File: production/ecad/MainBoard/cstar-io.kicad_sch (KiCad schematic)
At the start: 8 parts, among them J1 691137710002, J5 Conn_01x04_Socket, Q2 AO3400A, Q8 IRFHM9331TRPBF

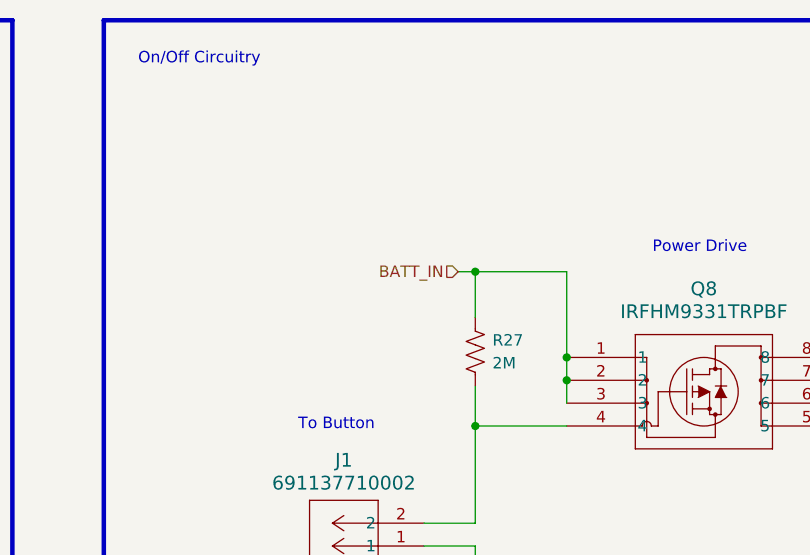
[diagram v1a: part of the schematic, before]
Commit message: updated battery connection net name
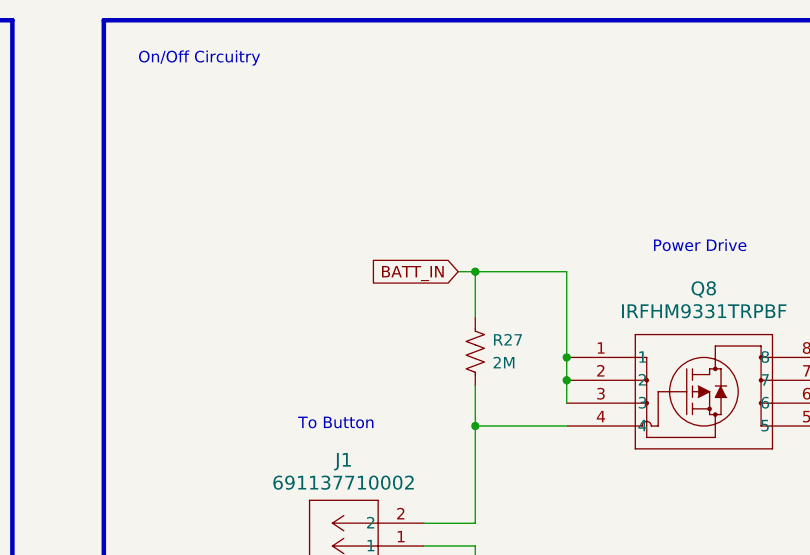
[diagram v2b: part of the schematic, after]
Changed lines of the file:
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@@
     (effects (font (size 1.27 1.27)) (justify left bottom))
+  )
+  (global_label "BATT_IN" (shape input) (at 196.85 43.815 180) (fields_autoplaced)
+    (effects (font (size 1.27 1.27)) (justify right))
+    (property "Intersheetrefs" "${INTERSHEET_REFS}" (at 186.6681 43.815 0)
+      (effects (font (size 1.27 1.27)) (justify right) hide)
+    )
   )
   (hierarchical_label "RGB_Red_Control" (shape input) (at 45.085 54.61 180) (fields_autoplaced)
@@
     (effects (font (size 1.27 1.27)) (justify right))
   )
-  (hierarchical_label "BATT_IN" (shape input) (at 196.85 43.815 180) (fields_autoplaced)
-    (effects (font (size 1.27 1.27)) (justify right))
-  )

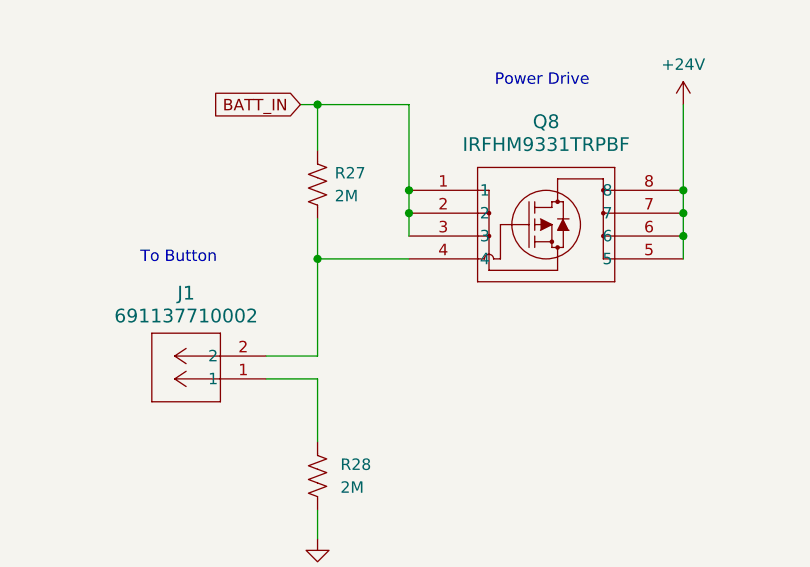
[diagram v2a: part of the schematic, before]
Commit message: added test point
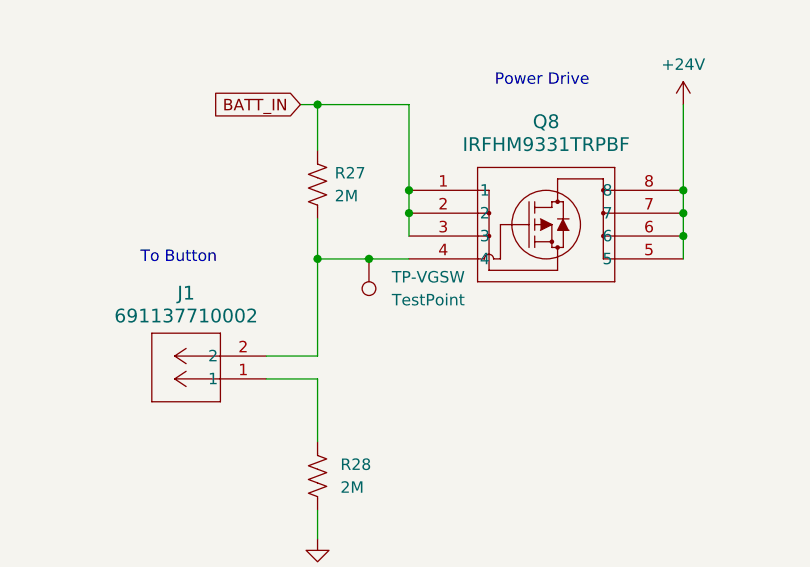
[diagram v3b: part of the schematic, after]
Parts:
- added TP-VGSW: TestPoint, symbol Connector:TestPoint
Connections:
- net at J1.2, Q8.4, R27.2: now also TP-VGSW.1
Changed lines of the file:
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@@
   (junction (at 239.395 55.88) (diameter 0) (color 0 0 0 0)
   )
+  (junction (at 204.47 60.96) (diameter 0) (color 0 0 0 0)
+  )
   (junction (at 208.915 55.88) (diameter 0) (color 0 0 0 0)
   )
@@
     (stroke (width 0.5) (type default))
   )
-  (wire (pts (xy 198.755 60.96) (xy 208.915 60.96))
+  (wire (pts (xy 198.755 60.96) (xy 204.47 60.96))
     (stroke (width 0) (type default))
   )
   (wire (pts (xy 239.395 55.88) (xy 239.395 58.42))
+    (stroke (width 0) (type default))
+  )
+  (wire (pts (xy 204.47 60.96) (xy 208.915 60.96))
     (stroke (width 0) (type default))
   )
@@
         )
       )
+    )
+  )
+  (symbol (lib_id "Connector:TestPoint") (at 204.47 60.96 180) (unit 1)
+    (in_bom yes) (on_board yes) (dnp no) (fields_autoplaced)
+    (property "Reference" "TP-VGSW" (at 207.01 62.992 0)
+      (effects (font (size 1.27 1.27)) (justify right))
+    )
+    (property "Value" "TestPoint" (at 207.01 65.532 0)
+      (effects (font (size 1.27 1.27)) (justify right))
+    )
+    (property "Footprint" "" (at 199.39 60.96 0)
+      (effects (font (size 1.27 1.27)) hide)
+    )
+    (property "Datasheet" "~" (at 199.39 60.96 0)
+      (effects (font (size 1.27 1.27)) hide)
+    )
+    (pin "1")
+    (instances
+      (project "CSTAR"
+        (path "/cd9fa943-c6eb-468b-990c-ea873c442553/222d3537-e437-4ced-92e0-9423c8895d91"
+          (reference "TP-VGSW") (unit 1)
+        )
+      )

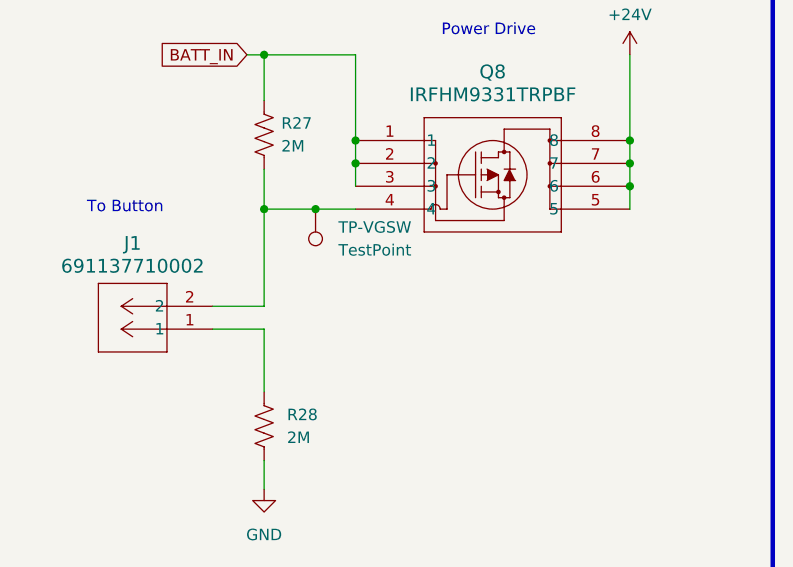
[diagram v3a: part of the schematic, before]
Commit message: added cap and fixed pmos symbol
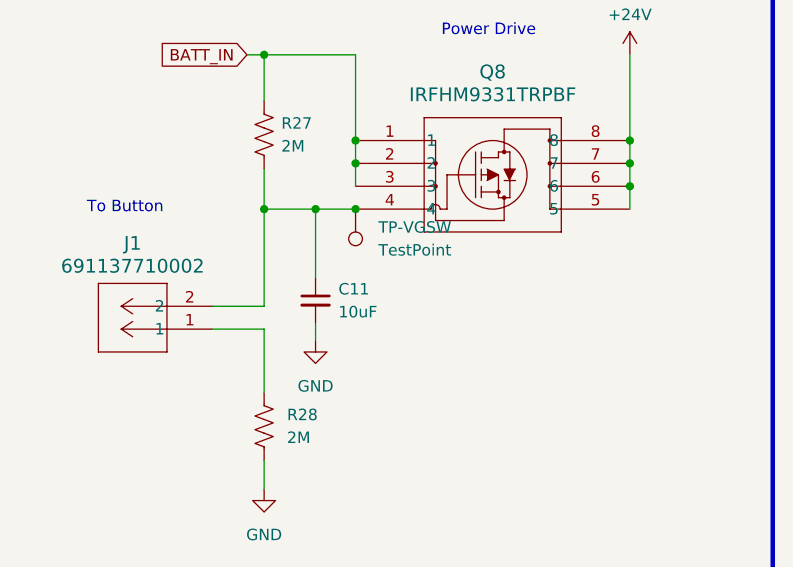
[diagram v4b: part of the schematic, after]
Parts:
- added C11: 10uF, symbol Device:C_Small
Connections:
- net GND: now also C11.2
- net at J1.2, Q8.4, R27.2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: now also C11.1
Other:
- moved on the sheet: TP-VGSW
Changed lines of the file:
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@@
   (junction (at 198.755 60.96) (diameter 0) (color 0 0 0 0)
   )
+  (junction (at 204.47 60.96) (diameter 0) (color 0 0 0 0)
+  )
   (junction (at 239.395 55.88) (diameter 0) (color 0 0 0 0)
   )
-  (junction (at 204.47 60.96) (diameter 0) (color 0 0 0 0)
-  )
   (junction (at 208.915 55.88) (diameter 0) (color 0 0 0 0)
   )
   (junction (at 239.395 58.42) (diameter 0) (color 0 0 0 0)
   )
+  (junction (at 208.915 60.96) (diameter 0) (color 0 0 0 0)
+  )
   (junction (at 239.395 53.34) (diameter 0) (color 0 0 0 0)
   )
@@
     (stroke (width 0) (type default))
   )
+  (wire (pts (xy 204.47 60.96) (xy 208.915 60.96))
+    (stroke (width 0) (type default))
+  )
   (polyline (pts (xy 147.32 112.395) (xy 147.32 15.875))
     (stroke (width 0.5) (type default))
@@
     (stroke (width 0.5) (type default))
   )
+  (wire (pts (xy 204.47 73.66) (xy 204.47 75.565))
+    (stroke (width 0) (type default))
+  )
   (wire (pts (xy 198.755 43.815) (xy 196.85 43.815))
     (stroke (width 0) (type default))
@@
     (stroke (width 0) (type default))
   )
+  (wire (pts (xy 204.47 60.96) (xy 204.47 68.58))
+    (stroke (width 0) (type default))
+  )
   (wire (pts (xy 208.915 55.88) (xy 208.915 53.34))
     (stroke (width 0) (type default))
@@
   )
   (wire (pts (xy 239.395 55.88) (xy 239.395 58.42))
-    (stroke (width 0) (type default))
-  )
-  (wire (pts (xy 204.47 60.96) (xy 208.915 60.96))
     (stroke (width 0) (type default))
   )
@@
     )
   )
+  (symbol (lib_id "Device:C_Small") (at 204.47 71.12 0) (unit 1)
+    (in_bom yes) (on_board yes) (dnp no) (fields_autoplaced)
+    (property "Reference" "C11" (at 207.01 69.8563 0)
+      (effects (font (size 1.27 1.27)) (justify left))
+    )
+    (property "Value" "10uF" (at 207.01 72.3963 0)
+      (effects (font (size 1.27 1.27)) (justify left))
+    )
+    (property "Footprint" "" (at 204.47 71.12 0)
+      (effects (font (size 1.27 1.27)) hide)
+    )
+    (property "Datasheet" "~" (at 204.47 71.12 0)
+      (effects (font (size 1.27 1.27)) hide)
+    )
+    (pin "2")
+    (pin "1")
+    (instances
+      (project "CSTAR"
+        (path "/cd9fa943-c6eb-468b-990c-ea873c442553/222d3537-e437-4ced-92e0-9423c8895d91"
+          (reference "C11") (unit 1)
+        )
+      )
+    )
+  )
   (symbol (lib_id "power:+24V") (at 239.395 43.815 0) (unit 1)
     (in_bom yes) (on_board yes) (dnp no) (fields_autoplaced)
@@
     )
   )
-  (symbol (lib_id "Connector:TestPoint") (at 204.47 60.96 180) (unit 1)
-    (in_bom yes) (on_board yes) (dnp no) (fields_autoplaced)
-    (property "Reference" "TP-VGSW" (at 207.01 62.992 0)
+  (symbol (lib_id "Connector:TestPoint") (at 208.915 60.96 180) (unit 1)
+    (in_bom yes) (on_board yes) (dnp no) (fields_autoplaced)
+    (property "Reference" "TP-VGSW" (at 211.455 62.992 0)
       (effects (font (size 1.27 1.27)) (justify right))
     )
-    (property "Value" "TestPoint" (at 207.01 65.532 0)
+    (property "Value" "TestPoint" (at 211.455 65.532 0)
       (effects (font (size 1.27 1.27)) (justify right))
     )
-    (property "Footprint" "" (at 199.39 60.96 0)
-      (effects (font (size 1.27 1.27)) hide)
-    )
-    (property "Datasheet" "~" (at 199.39 60.96 0)
+    (property "Footprint" "" (at 203.835 60.96 0)
+      (effects (font (size 1.27 1.27)) hide)
+    )
+    (property "Datasheet" "~" (at 203.835 60.96 0)
       (effects (font (size 1.27 1.27)) hide)
     )
@@
         )
       )
+    )
+  )
+  (symbol (lib_id "power:GND") (at 204.47 75.565 0) (unit 1)
+    (in_bom yes) (on_board yes) (dnp no) (fields_autoplaced)
+    (property "Reference" "#PWR045" (at 204.47 81.915 0)
+      (effects (font (size 1.27 1.27)) hide)
+    )
+    (property "Value" "GND" (at 204.47 80.645 0)
+      (effects (font (size 1.27 1.27)))
+    )
+    (property "Footprint" "" (at 204.47 75.565 0)
+      (effects (font (size 1.27 1.27)) hide)
+    )
+    (property "Datasheet" "" (at 204.47 75.565 0)
+      (effects (font (size 1.27 1.27)) hide)
+    )
+    (pin "1")
+    (instances
+      (project "CSTAR"
+        (path "/cd9fa943-c6eb-468b-990c-ea873c442553/222d3537-e437-4ced-92e0-9423c8895d91"
+          (reference "#PWR045") (unit 1)
+        )
+      )

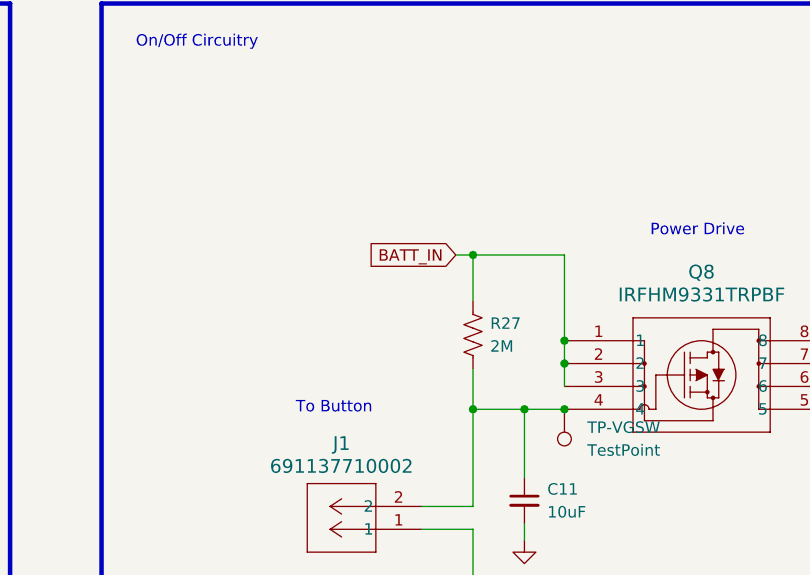
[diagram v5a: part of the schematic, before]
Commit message: Added TVS Diode, NC flags, diode to i/o, LEDs to each power rail
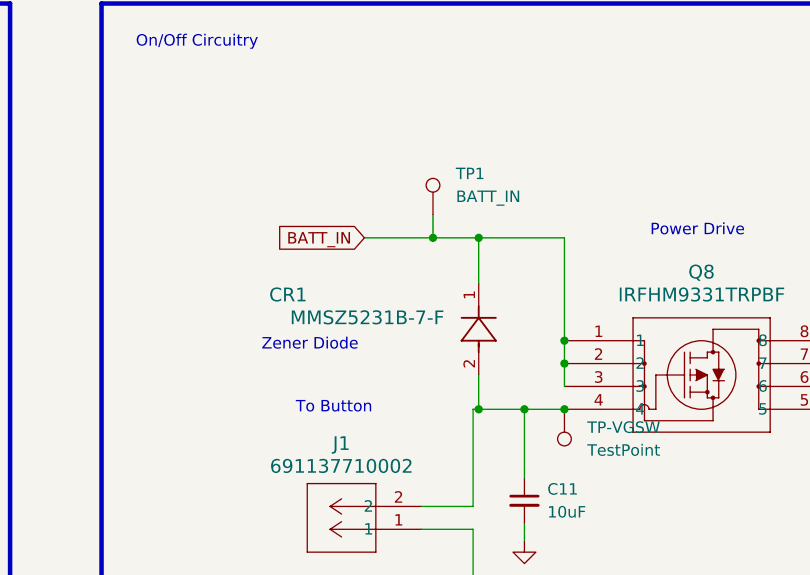
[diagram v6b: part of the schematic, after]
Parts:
- removed R27: 2M, symbol Device:R_US
- added CR1: MMSZ5231B-7-F, SOD123_DIO, symbol 2024-02-24_22-47-34:MMSZ5231B-7-F
- added TP1: BATT_IN, symbol Connector:TestPoint
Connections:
- net BATT_IN: now also CR1.1, TP1.1
- net at C11.1, J1.2, Q8.4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: now also CR1.2
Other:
- note added: "Zener Diode"
